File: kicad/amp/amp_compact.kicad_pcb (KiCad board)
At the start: 2 copper layers, 100 x 85 mm, 112 parts, among them J1 DC 12V IN, J2 IN L-G-R, J3 SPK L, J4 SPK R, Q1001 BC547, Q1002 BC547, Q1003 BC557, Q1004 BD139, Q1005 BD140, Q1006 BC547, Q2001 BC547, Q2002 BC547, Q2003 BC557, Q2004 BD139, Q2005 BD140, Q2006 BC547

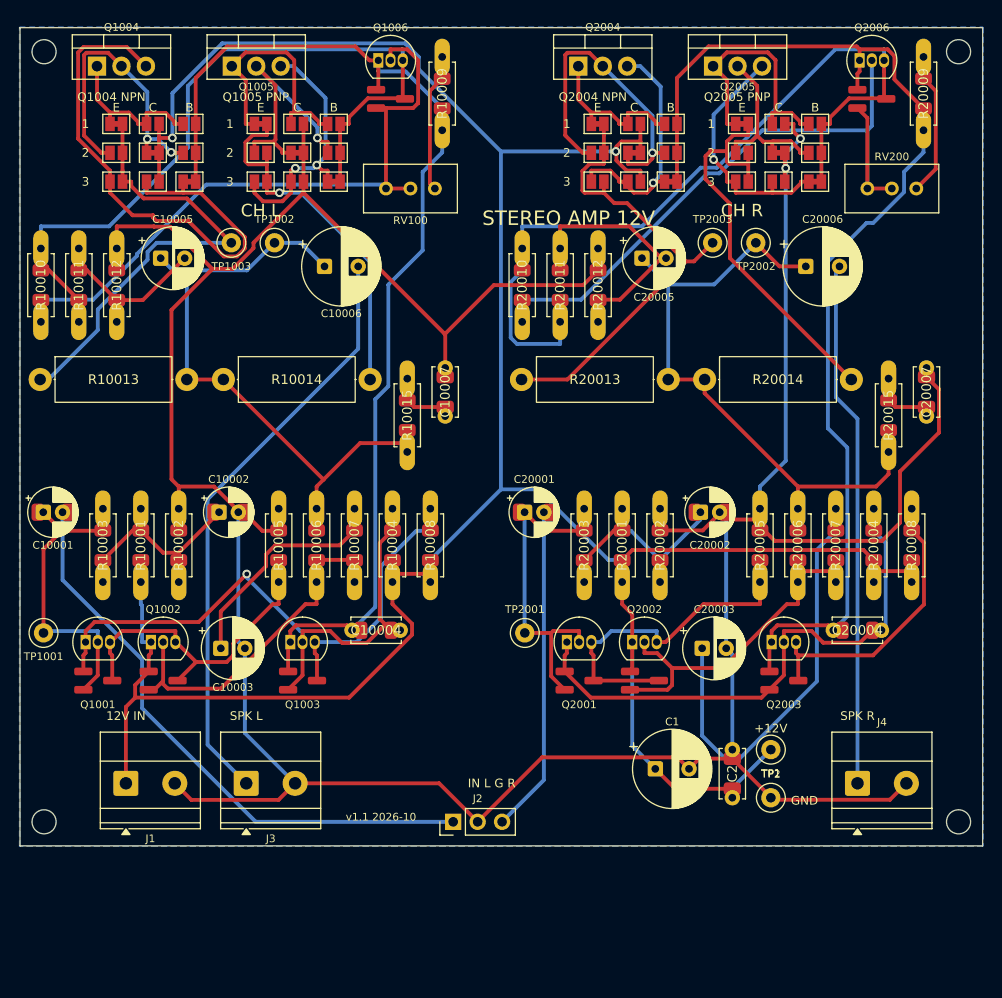
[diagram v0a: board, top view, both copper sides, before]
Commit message: Release 1.2: mirror-loaded front end, closed-loop PSU, VU tap, headphone board
- Amp: PNP input pair with NPN current-mirror load, LED-referenced current-source tail,
  NPN VAS with bootstrapped load from +12V, 220p Miller + 47p lead cap (THD 0.004% at 26 mW/8R,
  0.019% at 0.29 W; was 0.03 / 0.2). 1k VU meter tap per channel to header J5.
- PSU: BC547 error amplifier, 5.6 V zener fed from VOUT, 8.2k + 2k trimmer / 10k divider,
  2.2k drive, 47n/100n compensation. 12.0 V set point, 0.14 V dip on a 1 A step.
- New headphone board (DPDT switch, 120R series, DIRECT jumpers, 3.5 mm jack, panel-jack header).
- Boards: amp 134x85 / compact 100x98, PSU 90x58, hp 42x30; panel 155x155 with four boards.
  All 2-layer boards and the panel DRC clean; single-sided amp down to 15 errors.
- Toolchain: STAMP constant, reroute.sh second routing pass, rotated titles, link holes on
  jumper pads, 2 mm routing corridor per channel.
- Docs, BOMs, order guide, changelog, known issues rewritten for release 2.
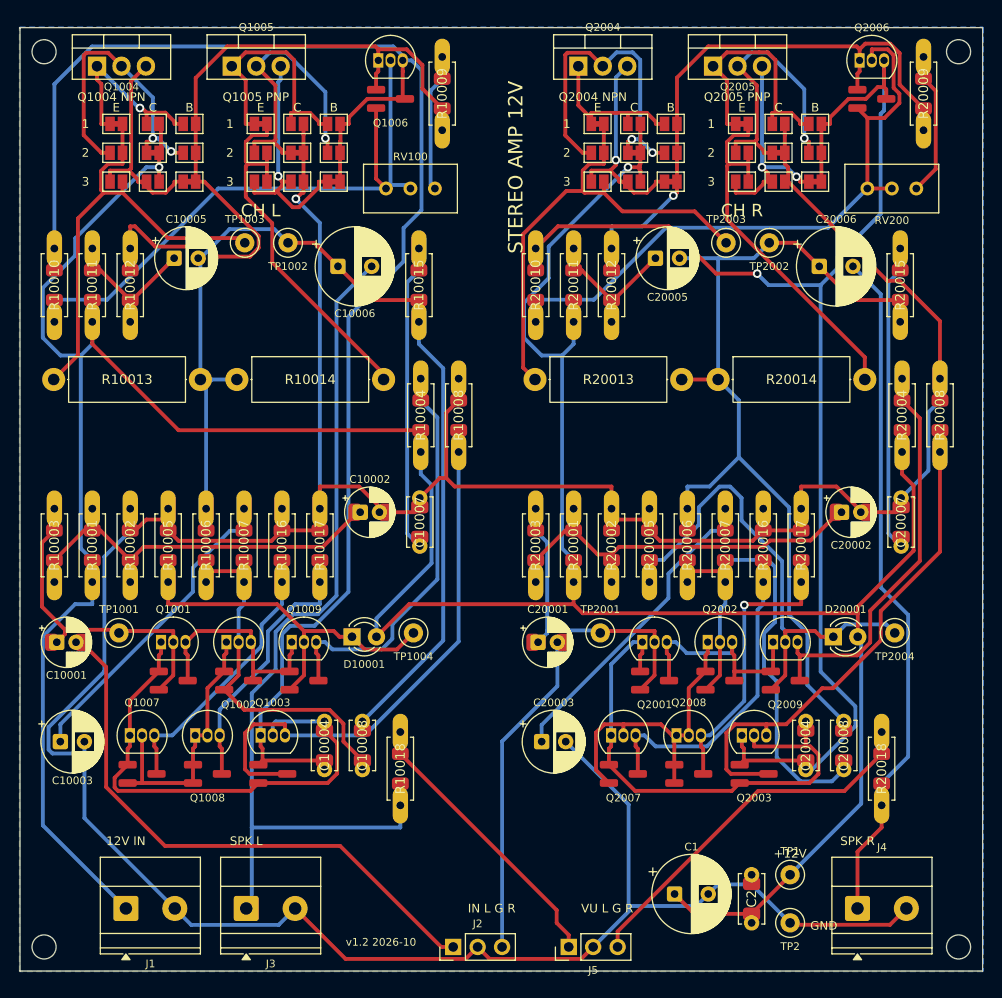
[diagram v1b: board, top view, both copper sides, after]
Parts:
- added C10008: 47p, Custom:C_P5_1206, F.Cu at (85.6, 127.1)
- added C20008: 47p, Custom:C_P5_1206, F.Cu at (135.6, 127.1)
- added D10001: LED red, LED_THT:LED_D3.0mm, F.Cu at (84.5, 113.3)
- added D20001: LED red, LED_THT:LED_D3.0mm, F.Cu at (134.5, 113.3)
- added J5: VU L-G-R, Connector_PinHeader_2.54mm:PinHeader_1x03_P2.54mm_Vertical, F.Cu at (107.0, 145.5)
- added Q1007: BC547, Custom:TO92_SOT23, F.Cu at (61.4, 123.5)
- added Q1008: BC547, Custom:TO92_SOT23, F.Cu at (68.2, 123.5)
- added Q1009: BC557, Custom:TO92_SOT23, F.Cu at (78.2, 113.8)
- added Q2007: BC547, Custom:TO92_SOT23, F.Cu at (111.4, 123.5)
- added Q2008: BC547, Custom:TO92_SOT23, F.Cu at (118.2, 123.5)
- added Q2009: BC557, Custom:TO92_SOT23, F.Cu at (128.2, 113.8)
- added R10016: 100, Custom:R_Axial_1206, F.Cu at (77.2, 107.6)
- added R10017: 100, Custom:R_Axial_1206, F.Cu at (81.2, 107.6)
- added R10018: 1k, Custom:R_Axial_1206, F.Cu at (89.5, 130.8)
- added R20016: 100, Custom:R_Axial_1206, F.Cu at (127.2, 107.6)
- added R20017: 100, Custom:R_Axial_1206, F.Cu at (131.2, 107.6)
- added R20018: 1k, Custom:R_Axial_1206, F.Cu at (139.5, 130.8)
- added TP1004: LED 10.2V, TestPoint:TestPoint_Loop_D2.50mm_Drill1.0mm, F.Cu at (90.9, 112.9)
- added TP2004: LED 10.2V, TestPoint:TestPoint_Loop_D2.50mm_Drill1.0mm, F.Cu at (140.9, 112.9)
- C10004, C20004: value 100p -> 220p
- Q1001, Q1002, Q2001, Q2002: value BC547 -> BC557
- Q1003, Q2003: value BC557 -> BC547
- R10004, R20004: value 4.7k -> 1.2k
- R10005, R20005: value 10k -> 4.7k
- TP1001, TP2001: value B1 5.9V -> B1 6.1V
- moved C10003 19.3 mm to (54.2, 124.2)
- moved C20003 19.3 mm to (104.2, 124.2)
- moved C20004 14.7 mm to (131.6, 127.1), turned to 90 degrees
- moved C10004 14.7 mm to (81.6, 127.1), turned to 90 degrees
- moved C10002 14.7 mm to (85.3, 100.3)
- moved C20002 14.7 mm to (135.3, 100.3)
- moved R10004 13.8 mm to (91.6, 94.1)
- moved R10008 13.8 mm to (95.6, 94.1)
- moved R20004 13.8 mm to (141.6, 94.1)
- moved R20008 13.8 mm to (145.6, 94.1)
- moved C10007 13.8 mm to (91.5, 103.9)
- moved C20007 13.8 mm to (141.5, 103.9)
- moved C10001 13.6 mm to (53.8, 113.8)
- moved C20001 13.6 mm to (103.8, 113.8)
- moved R20015 13.6 mm to (141.4, 80.6)
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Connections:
- C10004 pad 1: /VAS_L -> /B5_L
- C10004 pad 1S: /VAS_L -> /B5_L
- C10005 pad 1: /OUT_L -> Net-(C10005-Pad1)
- C10005 pad 2: Net-(C10005-Pad2) -> /OUT_L
- C20004 pad 1: /VAS_R -> /B5_R
- C20004 pad 1S: /VAS_R -> /B5_R
- C20005 pad 1: /OUT_R -> Net-(C20005-Pad1)
- C20005 pad 2: Net-(C20005-Pad2) -> /OUT_R
- Q1002 pad 1: +12V -> Net-(Q1002-C)
- Q1002 pad 1S: +12V -> Net-(Q1002-C)
- Q1003 pad 1: /VAS_L -> /B5_L
- Q1003 pad 1S: /VAS_L -> /B5_L
- Q2002 pad 1: +12V -> Net-(Q2002-C)
- Q2002 pad 1S: +12V -> Net-(Q2002-C)
- Q2003 pad 1: /VAS_R -> /B5_R
- Q2003 pad 1S: /VAS_R -> /B5_R
- R10004 pad 2: Net-(Q1001-C) -> Net-(Q1009-E)
- R10004 pad 2S: Net-(Q1001-C) -> Net-(Q1009-E)
- R10005 pad 1: Net-(Q1001-E) -> Net-(D10001-K)
- R10005 pad 1S: Net-(Q1001-E) -> Net-(D10001-K)
- R10008 pad 1: +12V -> Net-(Q1003-E)
- R10008 pad 1S: +12V -> Net-(Q1003-E)
- R10008 pad 2: Net-(Q1003-E) -> GND
- R10008 pad 2S: Net-(Q1003-E) -> GND
- R10011 pad 1: /B5_L -> +12V
- R10011 pad 1S: /B5_L -> +12V
- R10011 pad 2: Net-(C10005-Pad2) -> Net-(C10005-Pad1)
- R10011 pad 2S: Net-(C10005-Pad2) -> Net-(C10005-Pad1)
- R10012 pad 1: Net-(C10005-Pad2) -> Net-(C10005-Pad1)
- R10012 pad 1S: Net-(C10005-Pad2) -> Net-(C10005-Pad1)
- R10012 pad 2: GND -> /VAS_L
- R10012 pad 2S: GND -> /VAS_L
- R20004 pad 2: Net-(Q2001-C) -> Net-(Q2009-E)
- R20004 pad 2S: Net-(Q2001-C) -> Net-(Q2009-E)
- R20005 pad 1: Net-(Q2001-E) -> Net-(D20001-K)
- R20005 pad 1S: Net-(Q2001-E) -> Net-(D20001-K)
- R20008 pad 1: +12V -> Net-(Q2003-E)
- R20008 pad 1S: +12V -> Net-(Q2003-E)
- R20008 pad 2: Net-(Q2003-E) -> GND
- R20008 pad 2S: Net-(Q2003-E) -> GND
- R20011 pad 1: /B5_R -> +12V
- R20011 pad 1S: /B5_R -> +12V
- R20011 pad 2: Net-(C20005-Pad2) -> Net-(C20005-Pad1)
- R20011 pad 2S: Net-(C20005-Pad2) -> Net-(C20005-Pad1)
- R20012 pad 1: Net-(C20005-Pad2) -> Net-(C20005-Pad1)
- R20012 pad 1S: Net-(C20005-Pad2) -> Net-(C20005-Pad1)
- R20012 pad 2: GND -> /VAS_R
- R20012 pad 2S: GND -> /VAS_R
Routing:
- net /B5_L: track 80.4 -> 166.9 mm
- net +12V: track 292.3 -> 360.6 mm
- net /B5_R: track 88.9 -> 145.0 mm, vias 0 -> 1
- net /VAS_R: track 118.5 -> 63.3 mm, vias 0 -> 1
- net Net-(D20001-K): track 0.00 -> 54.9 mm
- net Net-(Q1009-E): track 0.00 -> 44.7 mm
- net Net-(Q2009-E): track 0.00 -> 42.3 mm
- net /OUT_L: track 67.7 -> 108.4 mm
- net Net-(D10001-K): track 0.00 -> 39.4 mm
- net /VU_R: track 0.00 -> 38.9 mm
- net /VAS_L: track 116.8 -> 78.1 mm
- net Net-(JP10007-A): track 56.9 -> 22.5 mm
- net Net-(Q2007-E): track 0.00 -> 33.7 mm
- net Net-(Q2002-C): track 0.00 -> 33.0 mm
- net /SPK_L: track 61.8 -> 93.6 mm
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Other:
- board size 100 x 85 mm -> 100 x 98 mm
- board text added: "STEREO AMP 12V compact 100 mm wide CC BY-NC-SA 4.0"
- board text added: "VU L G R"
- board text added: "github.com/lahirunirmalx/discrete-stereo-amp v1.2 2026-10"
- board text added: "v1.2 2026-10"
- board text removed: "STEREO AMP 12V compact 100 x 85 mm CC BY-NC-SA 4.0"
- board text removed: "github.com/lahirunirmalx/discrete-stereo-amp v1.1 2026-10"
- board text removed: "v1.1 2026-10"
